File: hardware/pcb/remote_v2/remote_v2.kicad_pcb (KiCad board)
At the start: 2 copper layers, 109.2 x 71.1 mm, 32 parts

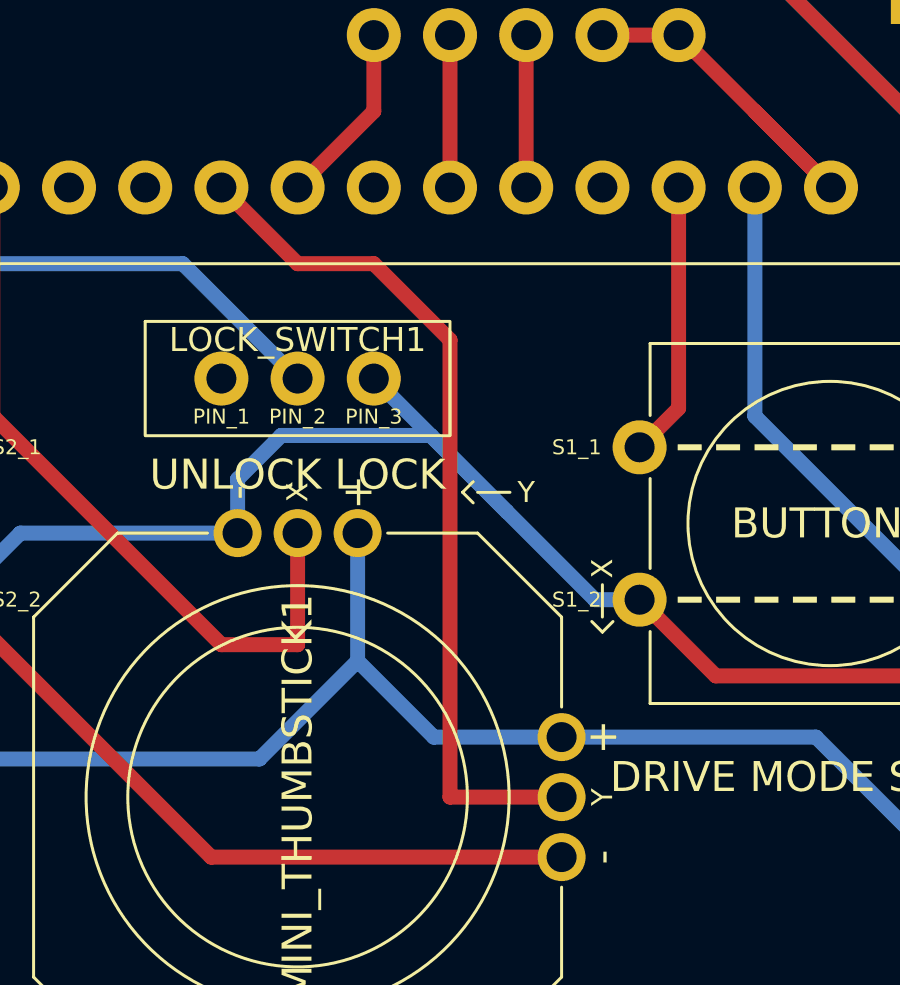
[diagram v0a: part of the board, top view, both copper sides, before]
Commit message: remote: Update PCB for remote.
Fix the issue that GPIO 35 does not have internal PULLUP resistor.
So switch the pin with the gimbal thumbstick input Y, instead of the
drive mode button.

Update sensor and tag pcb as well to reflect the changes.
- tag: Use pin 39 for battery measurement and revert the resistor value
  change that's done in the previous commit.
- sensor: Fix a wiring issue.
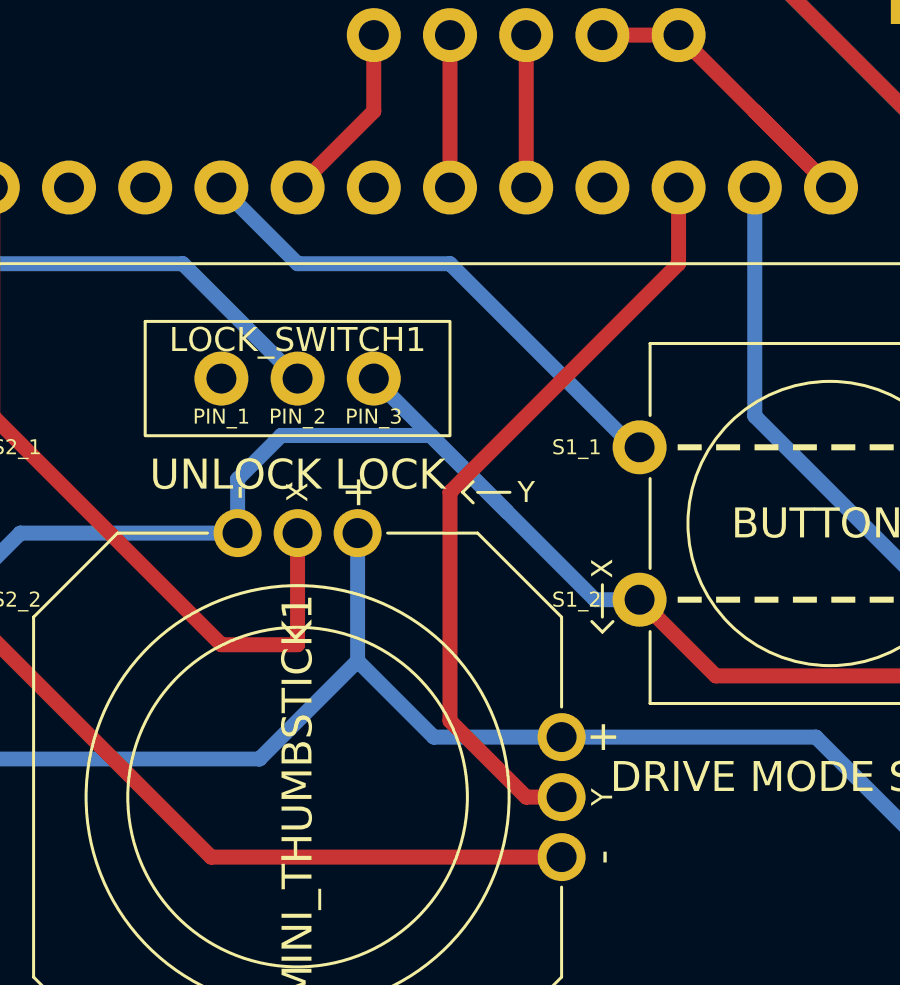
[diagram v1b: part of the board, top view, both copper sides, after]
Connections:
- ESP32_UWB1 pad 12: Net-(ESP32_UWB1-IO25) -> Net-(BUTTON1-S1_1)
- ESP32_UWB1 pad 18: Net-(BUTTON1-S1_1) -> Net-(ESP32_UWB1-IO35)
- MINI_THUMBSTICK1 pad 5: Net-(ESP32_UWB1-IO25) -> Net-(ESP32_UWB1-IO35)
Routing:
- net Net-(ESP32_UWB1-IO25): track 29.2 -> 0.00 mm
- net Net-(ESP32_UWB1-IO35): track 0.00 -> 25.7 mm
- net Net-(BUTTON1-S1_1): track 9.20 -> 18.0 mm
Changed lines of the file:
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@@
 	(net 5 "unconnected-(3.7V_BATTERY_CHARGER1-B--Pad5)")
 	(net 6 "Net-(3.7V_BATTERY_CHARGER1-OUT-)")
-	(net 7 "Net-(ESP32_UWB1-IO25)")
+	(net 7 "Net-(ESP32_UWB1-IO35)")
 	(net 8 "unconnected-(BUTTON2-S1_2-Pad2)")
 	(net 9 "Net-(ESP32_UWB1-3V3)")
@@
 			(layers "*.Cu" "*.Mask")
 			(remove_unused_layers no)
-			(net 7 "Net-(ESP32_UWB1-IO25)")
+			(net 66 "Net-(BUTTON1-S1_1)")
 			(pinfunction "IO25")
 			(pintype "bidirectional")
@@
 			(layers "*.Cu" "*.Mask")
 			(remove_unused_layers no)
-			(net 66 "Net-(BUTTON1-S1_1)")
+			(net 7 "Net-(ESP32_UWB1-IO35)")
 			(pinfunction "IO35")
 			(pintype "bidirectional")
@@
 			(layers "*.Cu" "*.Mask")
 			(remove_unused_layers no)
-			(net 7 "Net-(ESP32_UWB1-IO25)")
+			(net 7 "Net-(ESP32_UWB1-IO35)")
 			(pinfunction "Y")
 			(pintype "output")
@@
 	)
 	(segment
-		(start 147.32 104.14)
-		(end 149.86 104.14)
+		(start 160.02 101.6)
+		(end 160.02 104.14)
 		(width 0.5)
 		(layer "F.Cu")
@@
 	)
 	(segment
-		(start 144.78 101.6)
-		(end 147.32 104.14)
+		(start 152.4 111.76)
+		(end 152.4 119.38)
 		(width 0.5)
 		(layer "F.Cu")
@@
 	)
 	(segment
-		(start 152.4 121.92)
+		(start 154.94 121.92)
 		(end 156.12 121.92)
 		(width 0.5)
@@
 	)
 	(segment
-		(start 149.86 104.14)
-		(end 152.4 106.68)
+		(start 160.02 104.14)
+		(end 152.4 111.76)
 		(width 0.5)
 		(layer "F.Cu")
@@
 	)
 	(segment
-		(start 152.4 106.68)
-		(end 152.4 121.92)
+		(start 152.4 119.38)
+		(end 154.94 121.92)
 		(width 0.5)
 		(layer "F.Cu")
@@
 	)
 	(segment
-		(start 144.78 101.6)
-		(end 145.260182 101.6)
-		(width 0.3)
-		(layer "B.Cu")
-		(net 7)
-	)
-	(segment
 		(start 99.06 80.01)
 		(end 106.68 80.01)
@@
 	)
 	(segment
-		(start 160.02 108.960058)
-		(end 160.02 101.6)
+		(start 144.78 101.6)
+		(end 147.32 104.14)
 		(width 0.5)
-		(layer "F.Cu")
+		(layer "B.Cu")
 		(net 66)
 	)
 	(segment
-		(start 158.72 110.260058)
-		(end 160.02 108.960058)
+		(start 147.32 104.14)
+		(end 152.4 104.14)
 		(width 0.5)
-		(layer "F.Cu")
+		(layer "B.Cu")
+		(net 66)
+	)
+	(segment
+		(start 158.520058 110.260058)
+		(end 158.72 110.260058)
+		(width 0.5)
+		(layer "B.Cu")
+		(net 66)
+	)
+	(segment
+		(start 152.4 104.14)
+		(end 158.520058 110.260058)
+		(width 0.5)
+		(layer "B.Cu")
+		(net 66)
+	)
+	(segment
+		(start 144.78 101.6)
+		(end 145.260182 101.6)
+		(width 0.3)
+		(layer "B.Cu")
 		(net 66)
 	)
